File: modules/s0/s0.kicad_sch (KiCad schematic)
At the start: 0 parts

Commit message: chore: add production files
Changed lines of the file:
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@@
 	)
 	(sheet
-		(at 21.59 138.43)
+		(at 43.18 140.97)
 		(size 93.98 43.18)
 		(stroke
@@
 		)
 		(property "Sheetname" "WMBUS"
-			(at 47.244 162.56 0)
+			(at 68.834 165.1 0)
 			(effects
 				(font
 					(size 8 8)
+					(thickness 1.6)
+					(bold yes)
 				)
 				(justify left bottom)
@@
 		)
 		(property "Sheetfile" "wmbus.kicad_sch"
-			(at 21.59 182.1946 0)
+			(at 43.18 184.7346 0)
 			(effects
 				(font
@@
 	)
 	(sheet
-		(at 21.59 78.74)
+		(at 43.18 81.28)
 		(size 92.71 46.99)
 		(stroke
@@
 		)
 		(property "Sheetname" "MCU"
-			(at 52.07 107.188 0)
+			(at 73.66 109.728 0)
 			(effects
 				(font
 					(size 8 8)
+					(thickness 1.6)
+					(bold yes)
 				)
 				(justify left bottom)
@@
 		)
 		(property "Sheetfile" "mcu.kicad_sch"
-			(at 21.59 126.3146 0)
+			(at 43.18 128.8546 0)
 			(effects
 				(font
@@
 	)
 	(sheet
-		(at 138.684 17.526)
+		(at 169.164 20.066)
 		(size 93.472 45.466)
 		(stroke
@@
 		)
 		(property "Sheetname" "SIM7080G"
-			(at 142.24 45.72 0)
+			(at 177.546 49.784 0)
 			(effects
 				(font
@@
 		)
 		(property "Sheetfile" "peripherals.kicad_sch"
-			(at 138.684 63.5766 0)
+			(at 169.164 66.1166 0)
 			(effects
 				(font
@@
 	)
 	(sheet
-		(at 21.844 18.034)
+		(at 43.434 20.574)
 		(size 92.456 45.974)
 		(stroke
@@
 		)
 		(property "Sheetname" "Connector"
-			(at 24.384 46.736 0)
+			(at 57.404 49.276 0)
 			(effects
 				(font
@@
 		)
 		(property "Sheetfile" "connector.kicad_sch"
-			(at 21.844 64.5926 0)
+			(at 43.434 67.1326 0)
 			(effects
 				(font
@@
 	)
 	(sheet
-		(at 139.7 76.2)
+		(at 170.18 78.74)
 		(size 92.71 52.07)
 		(stroke
@@
 		)
 		(property "Sheetname" "LoRa"
-			(at 170.18 105.664 0)
+			(at 199.898 114.3 0)
 			(effects
 				(font
 					(size 8 8)
+					(thickness 1.6)
+					(bold yes)
 				)
 				(justify left bottom)
@@
 		)
 		(property "Sheetfile" "lora.kicad_sch"
-			(at 139.7 128.8546 0)
+			(at 170.18 131.3946 0)
 			(effects
 				(font

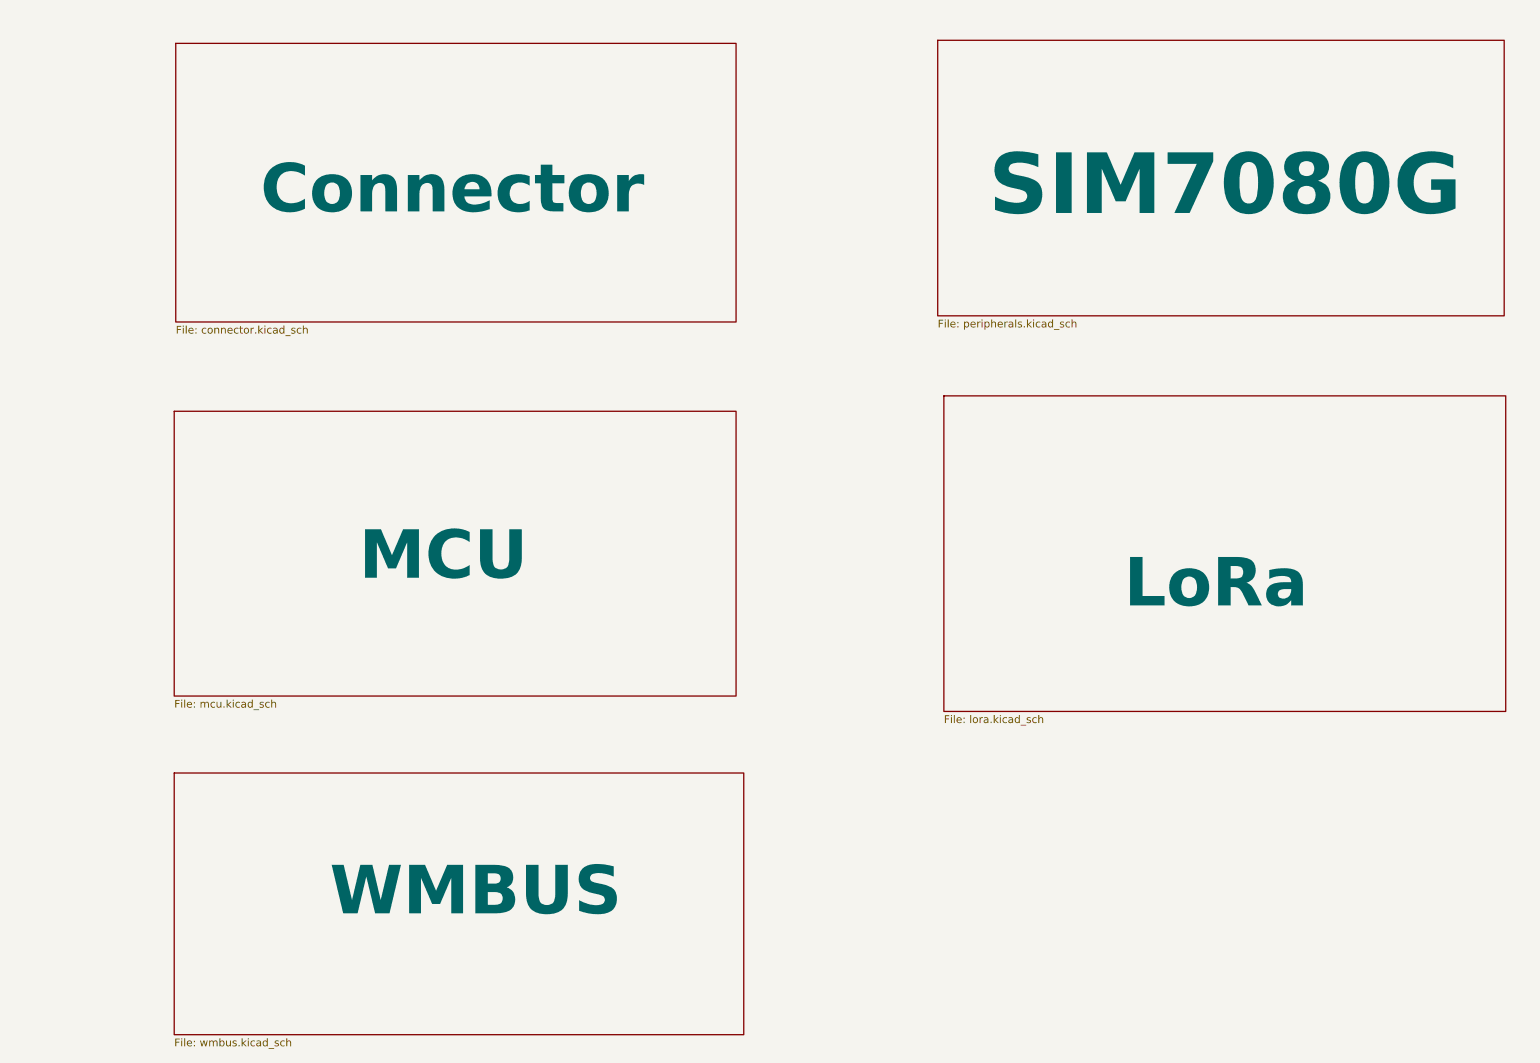
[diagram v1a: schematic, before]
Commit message: feat(s0): add GPIO mux for wired mbus and sd card
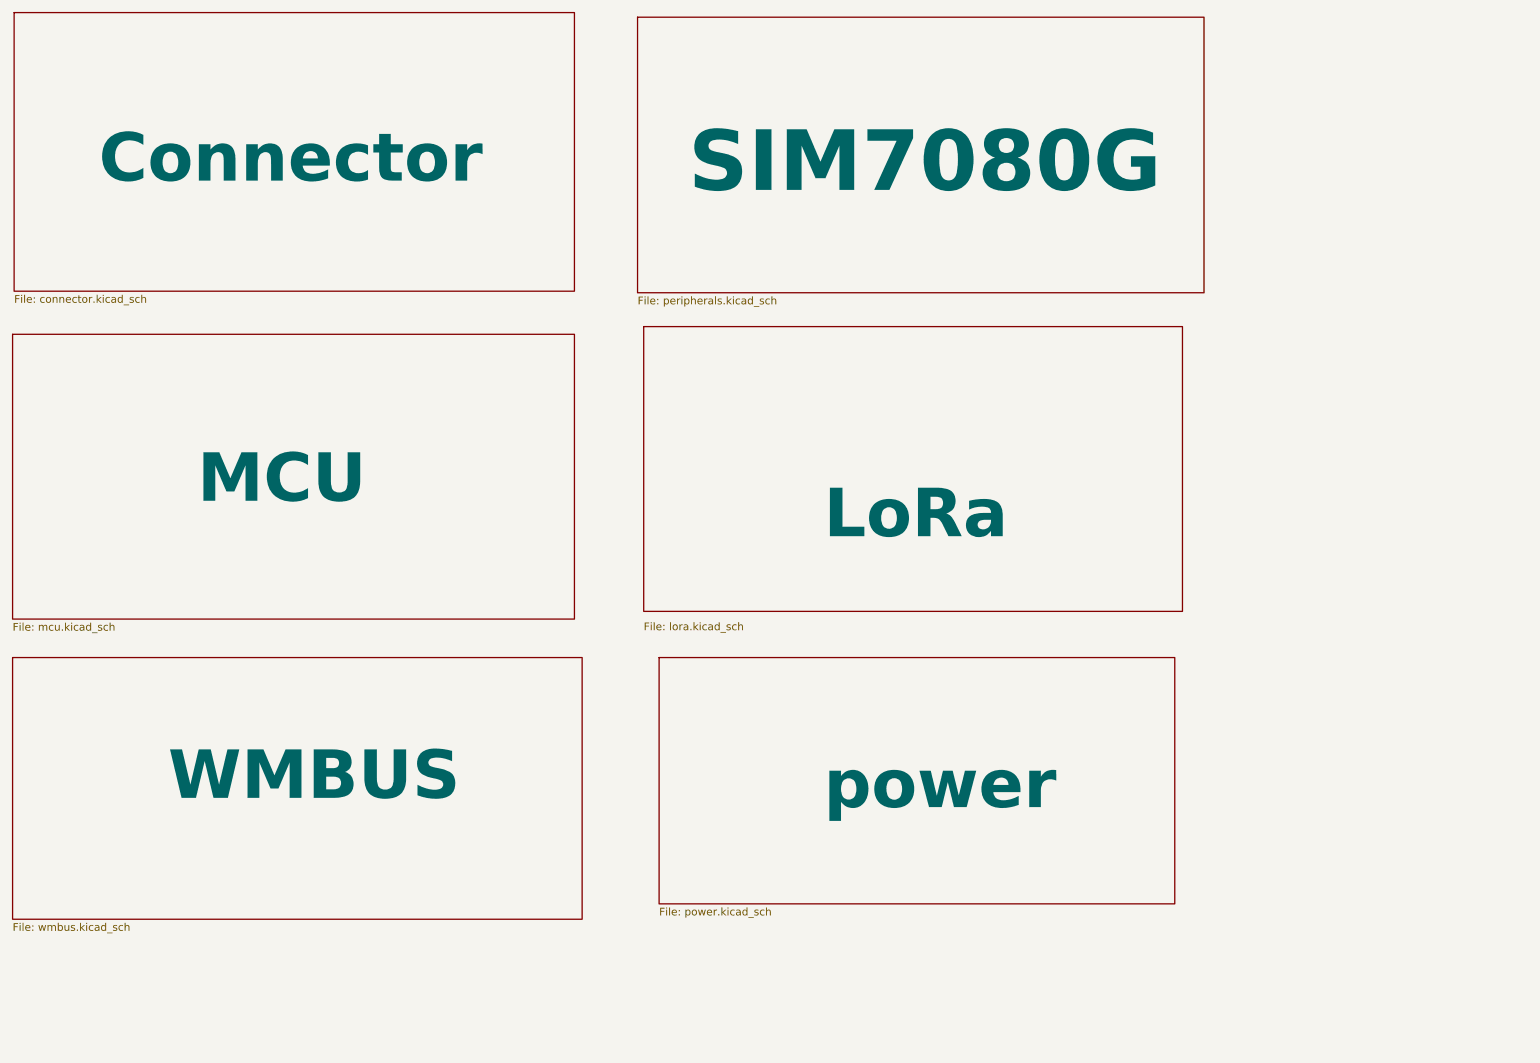
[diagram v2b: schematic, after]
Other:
- added sheet power (power.kicad_sch)
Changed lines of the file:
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@@
 	)
 	(sheet
-		(at 43.18 140.97)
+		(at 123.19 121.92)
+		(size 85.09 40.64)
+		(stroke
+			(width 0.1524)
+			(type solid)
+		)
+		(fill
+			(color 255 112 105 1.0000)
+		)
+		(property "Sheetname" "power"
+			(at 150.368 147.574 0)
+			(effects
+				(font
+					(size 8.001 8.001)
+					(thickness 1.6002)
+					(bold yes)
+				)
+				(justify left bottom)
+			)
+		)
+		(property "Sheetfile" "power.kicad_sch"
+			(at 123.19 163.1446 0)
+			(effects
+				(font
+					(size 1.27 1.27)
+				)
+				(justify left top)
+			)
+		)
+		(instances
+			(project "s0"
+				(path "/9e4c0f80-14bc-451b-8b05-b2f0d1a90e15"
+					(page "7")
+				)
+			)
+		)
+	)
+	(sheet
+		(at 16.51 121.92)
 		(size 93.98 43.18)
 		(stroke
@@
 		)
 		(property "Sheetname" "WMBUS"
-			(at 68.834 165.1 0)
+			(at 42.164 146.05 0)
 			(effects
 				(font
@@
 		)
 		(property "Sheetfile" "wmbus.kicad_sch"
-			(at 43.18 184.7346 0)
+			(at 16.51 165.6846 0)
 			(effects
 				(font
@@
 	)
 	(sheet
-		(at 43.18 81.28)
+		(at 16.51 68.58)
 		(size 92.71 46.99)
 		(stroke
@@
 		)
 		(property "Sheetname" "MCU"
-			(at 73.66 109.728 0)
+			(at 46.99 97.028 0)
 			(effects
 				(font
@@
 		)
 		(property "Sheetfile" "mcu.kicad_sch"
-			(at 43.18 128.8546 0)
+			(at 16.51 116.1546 0)
 			(effects
 				(font
@@
 	)
 	(sheet
-		(at 169.164 20.066)
+		(at 119.634 16.256)
 		(size 93.472 45.466)
 		(stroke
@@
 		)
 		(property "Sheetname" "SIM7080G"
-			(at 177.546 49.784 0)
+			(at 128.016 45.974 0)
 			(effects
 				(font
@@
 		)
 		(property "Sheetfile" "peripherals.kicad_sch"
-			(at 169.164 66.1166 0)
+			(at 119.634 62.3066 0)
 			(effects
 				(font
@@
 	)
 	(sheet
-		(at 43.434 20.574)
+		(at 16.764 15.494)
 		(size 92.456 45.974)
 		(stroke
@@
 		)
 		(fill
-			(color 194 0 0 0.5000)
+			(color 194 0 108 0.5000)
 		)
 		(property "Sheetname" "Connector"
-			(at 57.404 49.276 0)
+			(at 30.734 44.196 0)
 			(effects
 				(font
@@
 		)
 		(property "Sheetfile" "connector.kicad_sch"
-			(at 43.434 67.1326 0)
+			(at 16.764 62.0526 0)
 			(effects
 				(font
@@
 	)
 	(sheet
-		(at 170.18 78.74)
-		(size 92.71 52.07)
+		(at 120.65 67.31)
+		(size 88.9 46.99)
 		(stroke
 			(width 0.1524)
@@
 		)
 		(property "Sheetname" "LoRa"
-			(at 199.898 114.3 0)
+			(at 150.368 102.87 0)
 			(effects
 				(font
@@
 		)
 		(property "Sheetfile" "lora.kicad_sch"
-			(at 170.18 131.3946 0)
-			(effects
-				(font
+			(at 120.65 116.078 0)
+			(effects
+				(font

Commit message: wip: rework s0
Signed-off-by: Rodney Osodo <socials@rodneyosodo.com>
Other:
- removed sheet LoRa
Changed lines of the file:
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@@
 (kicad_sch
-	(version 20231120)
+	(version 20250114)
 	(generator "eeschema")
-	(generator_version "8.0")
+	(generator_version "9.0")
 	(paper "A4")
 	(title_block
@@
 		(at 123.19 121.92)
 		(size 85.09 40.64)
+		(exclude_from_sim no)
+		(in_bom yes)
+		(on_board yes)
+		(dnp no)
 		(stroke
 			(width 0.1524)
@@
 		(at 16.51 121.92)
 		(size 93.98 43.18)
+		(exclude_from_sim no)
+		(in_bom yes)
+		(on_board yes)
+		(dnp no)
 		(stroke
 			(width 0.1524)
@@
 		(at 16.51 68.58)
 		(size 92.71 46.99)
+		(exclude_from_sim no)
+		(in_bom yes)
+		(on_board yes)
+		(dnp no)
 		(stroke
 			(width 0.1524)
@@
 		(at 119.634 16.256)
 		(size 93.472 45.466)
+		(exclude_from_sim no)
+		(in_bom yes)
+		(on_board yes)
+		(dnp no)
 		(stroke
 			(width 0.1524)
@@
 		(at 16.764 15.494)
 		(size 92.456 45.974)
+		(exclude_from_sim no)
+		(in_bom yes)
+		(on_board yes)
+		(dnp no)
 		(stroke
 			(width 0.1524)
@@
 				(path "/9e4c0f80-14bc-451b-8b05-b2f0d1a90e15"
 					(page "2")
-				)
-			)
-		)
-	)
-	(sheet
-		(at 120.65 67.31)
-		(size 88.9 46.99)
-		(stroke
-			(width 0.1524)
-			(type solid)
-		)
-		(fill
-			(color 163 255 202 1.0000)
-		)
-		(property "Sheetname" "LoRa"
-			(at 150.368 102.87 0)
-			(effects
-				(font
-					(size 8 8)
-					(thickness 1.6)
-					(bold yes)
-				)
-				(justify left bottom)
-			)
-		)
-		(property "Sheetfile" "lora.kicad_sch"
-			(at 120.65 116.078 0)
-			(effects
-				(font
-					(size 1.27 1.27)
-				)
-				(justify left top)
-			)
-		)
-		(instances
-			(project "s0"
-				(path "/9e4c0f80-14bc-451b-8b05-b2f0d1a90e15"
-					(page "5")
 				)
 			)
@@
 		)
 	)
+	(embedded_fonts no)
 )
